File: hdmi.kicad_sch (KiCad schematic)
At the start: 44 parts, among them J13 46756-1001, Q12 PJE138K, U43 NTS0102GT, U44 TPD4E05U06QDQARQ1, U45 TPD4E05U06QDQARQ1, U46 TPD4E05U06QDQARQ1

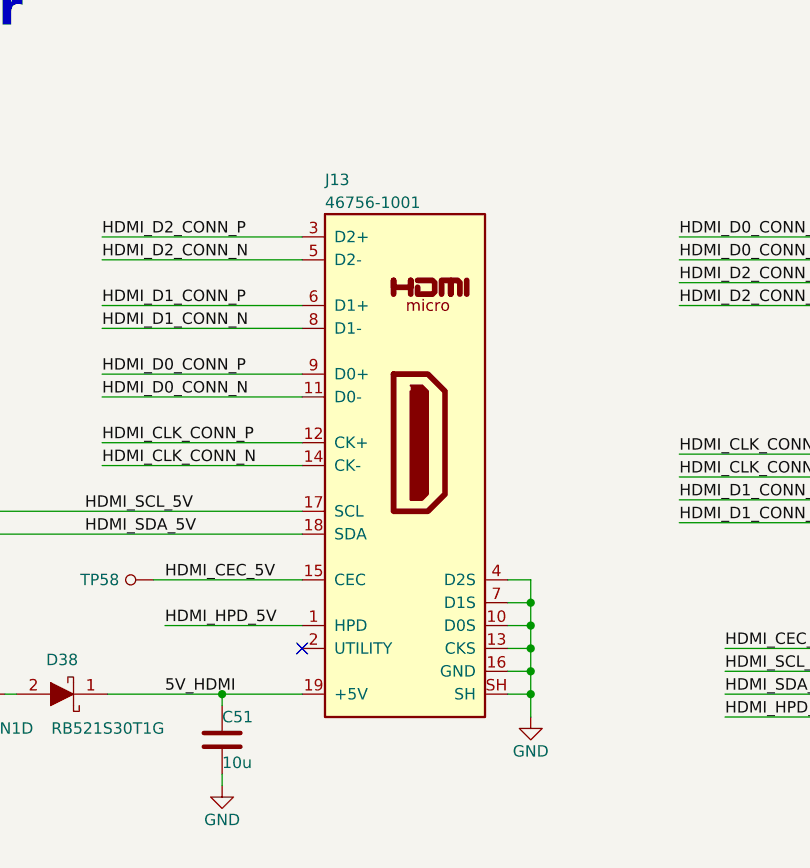
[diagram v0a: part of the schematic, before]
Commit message: Replace HDMI connector with mini HDMI one
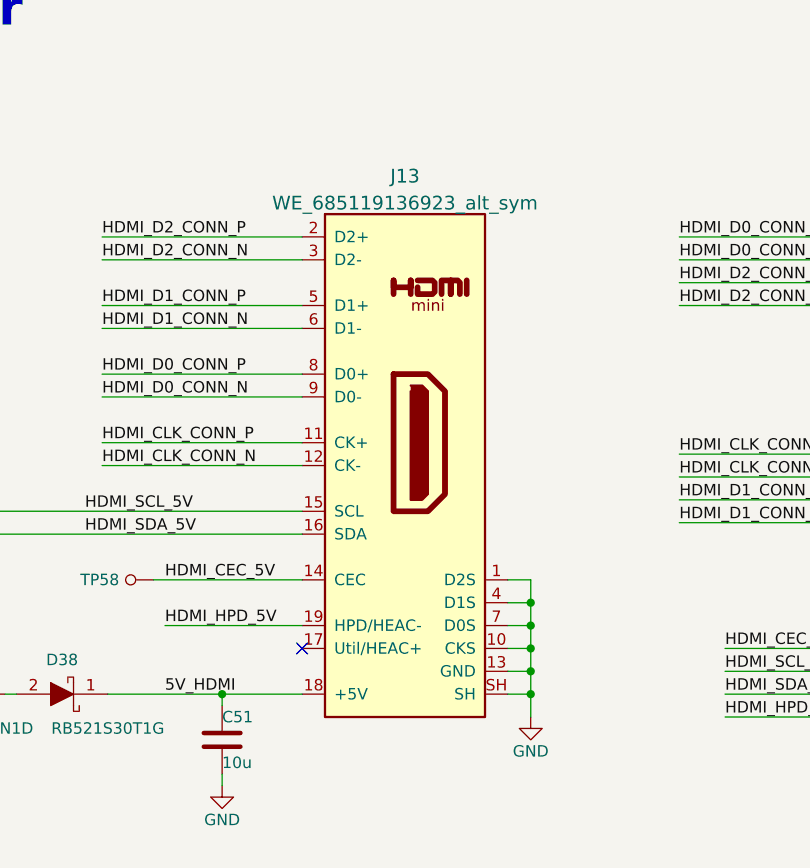
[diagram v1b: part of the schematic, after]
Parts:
- removed J13: 46756-1001, jetson-orin-baseboard-footprints:HDMI_Micro-D_Molex_46765-1x01, symbol jetson-orin-baseboard:46756-1001
- added J13: WE_685119136923_alt_sym, antmicro-footprints:WE_685119136923, symbol antmicroUSBDVIHDMIConnectors:WE_685119136923_alt_sym
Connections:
- net 5V_HDMI: now also J13.18 (+5V)
- net GND: now also J13.1 (D2S), J13.10 (CKS), J13.13 (GND), J13.4 (D1S), J13.7 (D0S), J13.SH
- net HDMI_CEC_5V: now also J13.14 (CEC)
- net HDMI_CLK_CONN_N: now also J13.12 (CK-)
- net HDMI_CLK_CONN_P: now also J13.11 (CK+)
- net HDMI_D0_CONN_N: now also J13.9 (D0-)
- net HDMI_D0_CONN_P: now also J13.8 (D0+)
- net HDMI_D1_CONN_N: now also J13.6 (D1-)
- net HDMI_D1_CONN_P: now also J13.5 (D1+)
- net HDMI_D2_CONN_N: now also J13.3 (D2-)
- net HDMI_D2_CONN_P: now also J13.2 (D2+)
- net HDMI_HPD_5V: now also J13.19 (HPD/HEAC-)
- net HDMI_SCL_5V: now also J13.15 (SCL)
- net HDMI_SDA_5V: now also J13.16 (SDA)
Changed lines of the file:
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@@
     (pin "1")
+  )
+  (symbol (lib_id "antmicroUSBDVIHDMIConnectors:WE_685119136923_alt_sym") (at 266.7 86.36 0) (unit 1)
+    (in_bom yes) (on_board yes) (fields_autoplaced)
+    (property "Reference" "J13" (id 0) (at 275.59 82.1489 0)
+      (effects (font (size 1.524 1.524)))
+    )
+    (property "Value" "WE_685119136923_alt_sym" (id 1) (at 275.59 85.1423 0)
+      (effects (font (size 1.524 1.524)))
+    )
+    (property "Footprint" "antmicro-footprints:WE_685119136923" (id 2) (at 289.56 147.32 0)
+      (effects (font (size 1.524 1.524)) hide)
+    )
+    (property "Datasheet" "" (id 3) (at 266.7 86.36 0)
+      (effects (font (size 1.524 1.524)) hide)
+    )
+    (property "Manufacturer" "Wurth Elektronik" (id 4) (at 274.32 149.86 0)
+      (effects (font (size 1.27 1.27)) hide)
+    )
+    (property "MPN" "685119136923" (id 5) (at 274.32 152.4 0)
+      (effects (font (size 1.27 1.27)) hide)
+    )
+    (pin "1")
+    (pin "10")
+    (pin "11")
+    (pin "12")
+    (pin "13")
+    (pin "14")
+    (pin "15")
+    (pin "16")
+    (pin "17")
+    (pin "18")
+    (pin "19")
+    (pin "2")
+    (pin "3")
+    (pin "4")
+    (pin "5")
+    (pin "6")
+    (pin "7")
+    (pin "8")
+    (pin "9")
+    (pin "SH")
   )
   (symbol (lib_id "jetson-orin-baseboard:NTS0102GT") (at 187.96 138.43 0) (unit 1)
@@
     (pin "2")
   )
-  (symbol (lib_id "jetson-orin-baseboard:46756-1001") (at 274.32 111.76 0) (unit 1)
-    (in_bom yes) (on_board yes)
-    (property "Reference" "J13" (id 0) (at 266.7 82.55 0)
-      (effects (font (size 1.27 1.27)) (justify left))
-    )
-    (property "Value" "46756-1001" (id 1) (at 266.7 85.0869 0)
-      (effects (font (size 1.27 1.27)) (justify left))
-    )
-    (property "Footprint" "jetson-orin-baseboard-footprints:HDMI_Micro-D_Molex_46765-1x01" (id 2) (at 274.32 147.32 0)
-      (effects (font (size 1.27 1.27)) hide)
-    )
-    (property "Datasheet" "https://www.molex.com/webdocs/datasheets/pdf/en-us/0467651001_IO_CONNECTORS.pdf" (id 3) (at 274.32 144.78 0)
-      (effects (font (size 1.27 1.27)) hide)
-    )
-    (property "MPN" "467651001" (id 4) (at 274.32 149.86 0)
-      (effects (font (size 1.27 1.27)) hide)
-    )
-    (property "Manufacturer" "Molex" (id 5) (at 274.32 152.4 0)
-      (effects (font (size 1.27 1.27)) hide)
-    )
-    (pin "1" (alternate "HPD"))
-    (pin "10")
-    (pin "11")
-    (pin "12")
-    (pin "13")
-    (pin "14")
-    (pin "15")
-    (pin "16")
-    (pin "17")
-    (pin "18")
-    (pin "19")
-    (pin "2" (alternate "UTILITY"))
-    (pin "3")
-    (pin "4")
-    (pin "5")
-    (pin "6")
-    (pin "7")
-    (pin "8")
-    (pin "9")
-    (pin "SH")
-  )
   (symbol (lib_id "jetson-orin-baseboard:R_2k2_0402") (at 250.19 171.45 90) (unit 1)

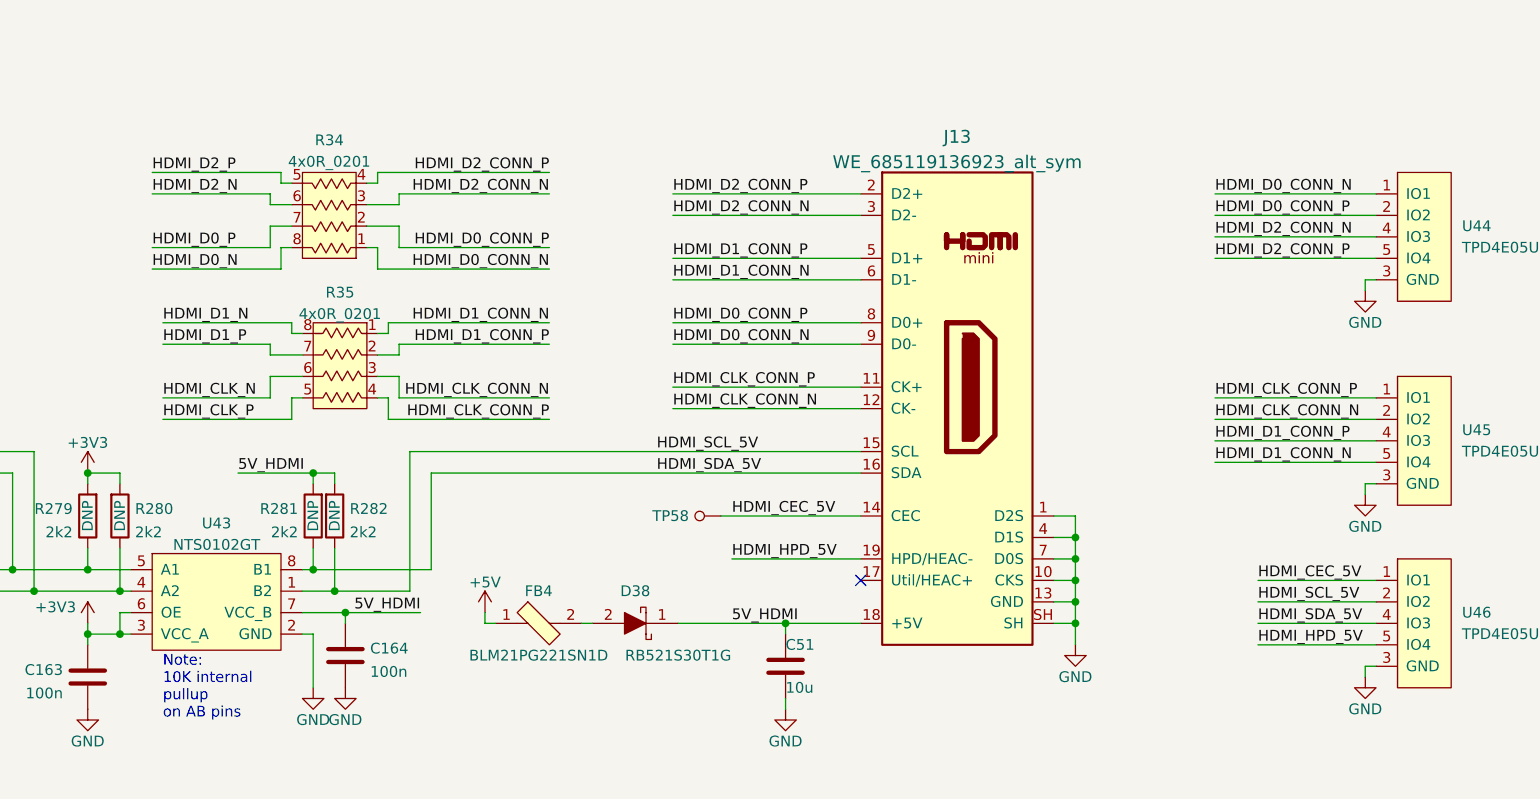
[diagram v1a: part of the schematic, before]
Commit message: Update pinout on passives to simplify routing
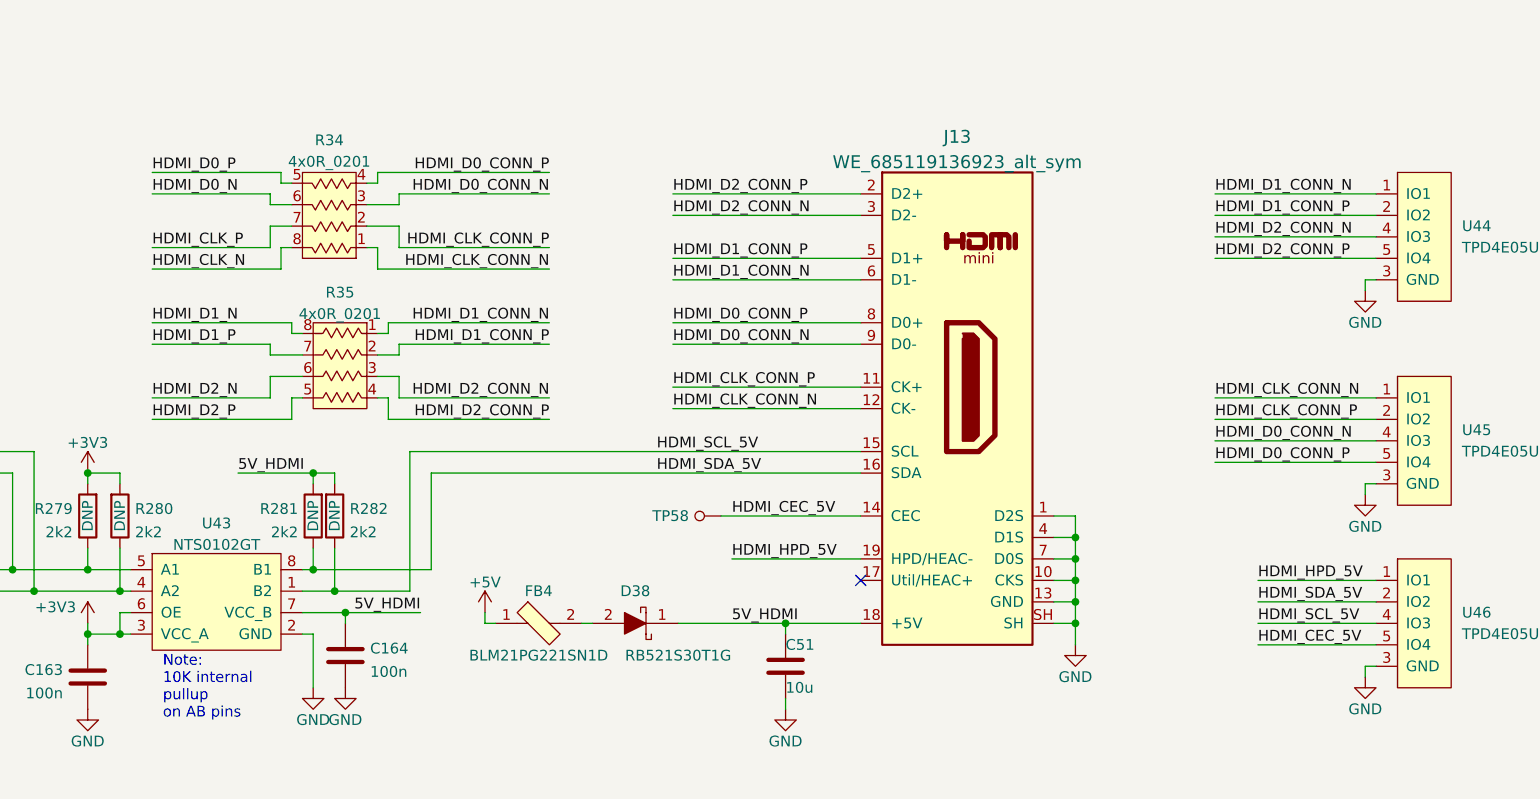
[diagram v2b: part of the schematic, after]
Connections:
- net HDMI_CEC_5V: now also U46.5 (IO4), U46.6 (IO4); no longer U46.1 (IO1), U46.10 (IO1)
- net HDMI_CLK_CONN_N: now also R34.1, U45.1 (IO1), U45.10 (IO1); no longer R35.3, U45.2 (IO2), U45.9 (IO2)
- net HDMI_CLK_CONN_P: now also R34.2, U45.2 (IO2), U45.9 (IO2); no longer R35.4, U45.1 (IO1), U45.10 (IO1)
- net HDMI_CLK_N: now also R34.8; no longer R35.6
- net HDMI_CLK_P: now also R34.7; no longer R35.5
- net HDMI_D0_CONN_N: now also R34.3, U45.4 (IO3), U45.7 (IO3); no longer R34.1, U44.1 (IO1), U44.10 (IO1)
- net HDMI_D0_CONN_P: now also R34.4, U45.5 (IO4), U45.6 (IO4); no longer R34.2, U44.2 (IO2), U44.9 (IO2)
- net HDMI_D0_N: now also R34.6; no longer R34.8
- net HDMI_D0_P: now also R34.5; no longer R34.7
- net HDMI_D1_CONN_N: now also U44.1 (IO1), U44.10 (IO1); no longer U45.5 (IO4), U45.6 (IO4)
- net HDMI_D1_CONN_P: now also U44.2 (IO2), U44.9 (IO2); no longer U45.4 (IO3), U45.7 (IO3)
- net HDMI_D2_CONN_N: now also R35.3; no longer R34.3
- net HDMI_D2_CONN_P: now also R35.4; no longer R34.4
- net HDMI_D2_N: now also R35.6; no longer R34.6
- net HDMI_D2_P: now also R35.5; no longer R34.5
- net HDMI_HPD_5V: now also U46.1 (IO1), U46.10 (IO1); no longer U46.5 (IO4), U46.6 (IO4)
- net HDMI_SCL_5V: now also U46.4 (IO3), U46.7 (IO3); no longer U46.2 (IO2), U46.9 (IO2)
- net HDMI_SDA_5V: now also U46.2 (IO2), U46.9 (IO2); no longer U46.4 (IO3), U46.7 (IO3)

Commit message: Use DP switch in place of selection via mounting option
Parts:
- removed C145, C146, C147, C148, C149, C150, C151, C152, C153, C154, C155, C156, C157, C158, C159, C160, C161, C162: C_100n_0402, jetson-orin-baseboard-footprints:0402-cap, symbol jetson-orin-baseboard:C_100n_0402
- removed R160: R_0R_0402, jetson-orin-baseboard-footprints:0402-res, symbol jetson-orin-baseboard:R_0R_0402
- removed R291: R_2k2_0402, jetson-orin-baseboard-footprints:0402-res, symbol jetson-orin-baseboard:R_2k2_0402
- added C131, C132, C133, C135, C136, C138, C139, C86, C87, C88, C92: C_100n_0402, jetson-orin-baseboard-footprints:0402-cap, symbol jetson-orin-baseboard:C_100n_0402
- added C47: C_1u_0402, jetson-orin-baseboard-footprints:0402-cap, symbol jetson-orin-baseboard:C_1u_0402
- added Q1: PJE138K, antmicro-footprints:SOT-523, symbol antmicroTransistorsFETsMOSFETsSingle:PJE138K
- added R160, R47, R49: R_10k_0402, jetson-orin-baseboard-footprints:0402-res, symbol jetson-orin-baseboard:R_10k_0402
- added R40: R_0R_0402, jetson-orin-baseboard-footprints:0402-res, symbol jetson-orin-baseboard:R_0R_0402
- added U36: TS3DV642RUARQ1, antmicro-footprints:WQFN-42-1EP_3.5x9mm_P0.5mm_EP2.05x7.55mm, symbol antmicroInterfaceAnalogSwitchesSpecialPurpose:TS3DV642RUARQ1
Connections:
- net HDMI_SDA_3V3 is gone; now on net HDMI_SCL_3V3: R278.2, R279.1, TP56.1, U43.5 (A1)
- net +1V8: now also Q1.1 (G), R47.2
- net +3V3: now also C136.2, C47.1, R160.2, R49.2, U36.1 (VCC)
- net DP1_AUX_N: now also C138.1
- net DP1_AUX_P: now also C139.1
- net DP1_HDMI_AUX_N: now also U36.4 (SDA/AUX-); no longer R278.1
- net DP1_HDMI_AUX_P: now also U36.3 (SCL/AUX+); no longer R277.1
- net DP1_HPD: now also R40.2
- net DP1_TXD0_HDMI_TX2_N: now also C86.2
- net DP1_TXD0_HDMI_TX2_P: now also C131.2
- net DP1_TXD0_N: now also U36.28 (D0-B)
- net DP1_TXD0_P: now also U36.29 (D0+B)
- net DP1_TXD1_HDMI_TX1_N: now also C87.2
- net DP1_TXD1_HDMI_TX1_P: now also C132.2
- net DP1_TXD1_N: now also U36.26 (D1-B)
- net DP1_TXD1_P: now also U36.27 (D1+B)
- net DP1_TXD2_HDMI_TX0_N: now also C88.2
- net DP1_TXD2_HDMI_TX0_P: now also C133.2
- net DP1_TXD2_N: now also U36.24 (D2-B)
- net DP1_TXD2_P: now also U36.25 (D2+B)
- net DP1_TXD3_HDMI_TXC_N: now also C92.2
- net DP1_TXD3_HDMI_TXC_P: now also C135.2
- net DP1_TXD3_N: now also U36.22 (D3-B)
- net DP1_TXD3_P: now also U36.23 (D3+B)
- net GND: now also C136.1, C47.2, U36.43 (GND)
- net HDMI_CLK_N: now also U36.31 (D3-A)
- net HDMI_CLK_P: now also U36.32 (D3+A)
- net HDMI_D0_N: now also U36.33 (D2-A)
- net HDMI_D0_P: now also U36.34 (D2+A)
- net HDMI_D1_N: now also U36.35 (D1-A)
- net HDMI_D1_P: now also U36.36 (D1+A)
- net HDMI_D2_N: now also U36.37 (D0-A)
- net HDMI_D2_P: now also U36.38 (D0+A)
- net at Q12.3 (D): now also U36.19 (HPD_A)
- new net: Q1.3 (D), R49.1, U36.14 (HPD)
- new net: Q1.2 (S), R40.1, R47.1
- new net DP_MUX_AUX_A+: R277.1, U36.42 (SCL/AUX+_A)
- new net DP_MUX_AUX_A-: R278.1, U36.41 (SDA/AUX-_A)
- new net DP_MUX_AUX_B+: C139.2, U36.40 (SCL/AUX+_B)
- new net DP_MUX_AUX_B-: C138.2, U36.39 (SDA/AUX-_B)
- new net DP_MUX_D0+: C131.1, U36.5 (D0+)
- new net DP_MUX_D0-: C86.1, U36.6 (D0-)
- new net DP_MUX_D1+: C132.1, U36.7 (D1+)
- new net DP_MUX_D1-: C87.1, U36.8 (D1-)
- new net DP_MUX_D2+: C133.1, C135.1, U36.10 (D2+), U36.12 (D3+)
- new net DP_MUX_D2-: C88.1, C92.1, U36.11 (D2-), U36.13 (D3-)
- new net DP_MUX_EN: R160.1, U36.2 (EN)
- new net USBC_HPD: U36.21 (HPD_B)
- no-connect marks 1 -> 3
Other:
- note removed: "Output selection"
- moved on the sheet: C163, C164, C51, D38, FB4, J13, Q12, R277, R278, R279, R280, R281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

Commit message: Routed DP++ signals to the display mux
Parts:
- removed C136: C_100n_0402, jetson-orin-baseboard-footprints:0402-cap, symbol jetson-orin-baseboard:C_100n_0402
- added R208: R_2k2_0402, jetson-orin-baseboard-footprints:0402-res, symbol jetson-orin-baseboard:R_2k2_0402
- added TP21: TP_SMD_0_75MM, jetson-orin-baseboard-footprints:Testpoint_smd_0_75mm, symbol jetson-orin-baseboard:TP_SMD_0_75MM
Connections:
- net +3V3: now also R208.2
- net DP1_HPD: now also TP21.1
- net DP1_TXD0_HDMI_TX2_N: now also C92.2; no longer C86.2
- net DP1_TXD0_HDMI_TX2_P: now also C135.2; no longer C131.2
- net DP1_TXD0_N: now also U36.31 (D3-A); no longer U36.28 (D0-B)
- net DP1_TXD0_P: now also U36.32 (D3+A); no longer U36.29 (D0+B)
- net DP1_TXD1_HDMI_TX1_N: now also C88.2; no longer C87.2
- net DP1_TXD1_HDMI_TX1_P: now also C133.2; no longer C132.2
- net DP1_TXD1_N: now also U36.33 (D2-A); no longer U36.26 (D1-B)
- net DP1_TXD1_P: now also U36.34 (D2+A); no longer U36.27 (D1+B)
- net DP1_TXD2_HDMI_TX0_N: now also C87.2; no longer C88.2
- net DP1_TXD2_HDMI_TX0_P: now also C132.2; no longer C133.2
- net DP1_TXD2_N: now also U36.35 (D1-A); no longer U36.24 (D2-B)
- net DP1_TXD2_P: now also U36.36 (D1+A); no longer U36.25 (D2+B)
- net DP1_TXD3_HDMI_TXC_N: now also C86.2; no longer C92.2
- net DP1_TXD3_HDMI_TXC_P: now also C131.2; no longer C135.2
- net DP1_TXD3_N: now also U36.37 (D0-A); no longer U36.22 (D3-B)
- net DP1_TXD3_P: now also U36.38 (D0+A); no longer U36.23 (D3+B)
- net DP_MUX_AUX_A+: now also U36.40 (SCL/AUX+_B); no longer U36.42 (SCL/AUX+_A)
- net DP_MUX_AUX_A-: now also U36.39 (SDA/AUX-_B); no longer U36.41 (SDA/AUX-_A)
- net DP_MUX_AUX_B+: now also U36.42 (SCL/AUX+_A); no longer U36.40 (SCL/AUX+_B)
- net DP_MUX_AUX_B-: now also U36.41 (SDA/AUX-_A); no longer U36.39 (SDA/AUX-_B)
- net DP_MUX_D2+: no longer C135.1, U36.12 (D3+)
- net DP_MUX_D2-: no longer C92.1, U36.13 (D3-)
- net HDMI_CLK_N: now also U36.28 (D0-B); no longer U36.31 (D3-A)
- net HDMI_CLK_P: now also U36.29 (D0+B); no longer U36.32 (D3+A)
- net HDMI_D0_N: now also U36.26 (D1-B); no longer U36.33 (D2-A)
- net HDMI_D0_P: now also U36.27 (D1+B); no longer U36.34 (D2+A)
- net HDMI_D1_N: now also U36.24 (D2-B); no longer U36.35 (D1-A)
- net HDMI_D1_P: now also U36.25 (D2+B); no longer U36.36 (D1+A)
- net HDMI_D2_N: now also U36.22 (D3-B); no longer U36.37 (D0-A)
- net HDMI_D2_P: now also U36.23 (D3+B); no longer U36.38 (D0+A)
- net HDMI_SCL_3V3: no longer R278.2, R280.1, TP57.1, U43.4 (A2)
- net USBC_HPD: now also U36.19 (HPD_A); no longer U36.21 (HPD_B)
- net at Q12.3 (D): now also U36.21 (HPD_B), R208.1; no longer U36.19 (HPD_A)
- new net DP_MUX_D3+: C135.1, U36.12 (D3+)
- new net DP_MUX_D3-: C92.1, U36.13 (D3-)
- new net HDMI_SDA_3V3: R278.2, R280.1, TP57.1, U43.4 (A2)
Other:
- moved on the sheet: C138, C139, C163, C164, C47, C51, D38, FB4, J13, Q1, Q12, R160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
